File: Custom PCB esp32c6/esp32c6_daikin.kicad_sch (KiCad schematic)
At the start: 24 parts, among them J2 Conn_01x05, Q1 BSS138PS, U1 TPS562246, U2 XIAO-ESP32-C6

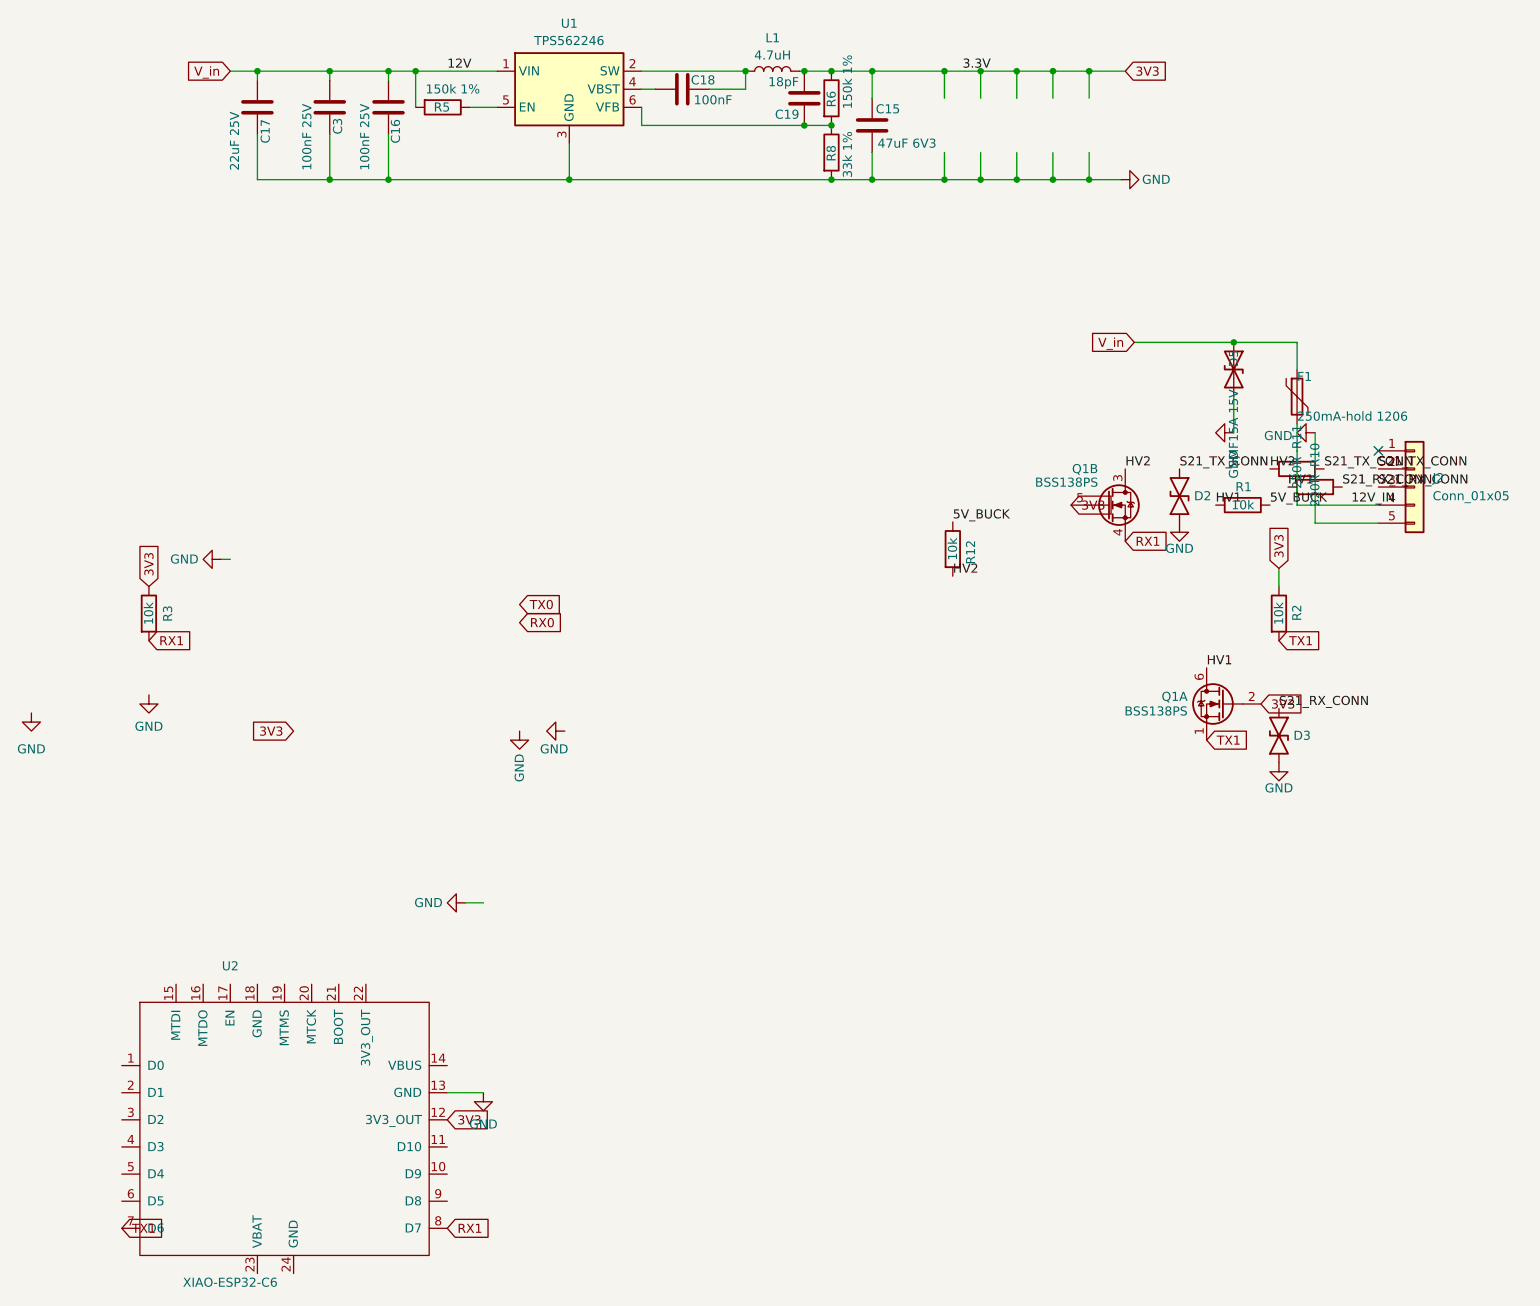
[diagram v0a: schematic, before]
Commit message: feat(xiao-sch): buck 5V re-tune, VBUS isolation diode, cap re-home
Re-tune TPS562246 buck 3.3V->5.0V, split the merged 3V3 net, add the
USB-back-feed isolation Schottky, and clear all ERC errors (29->0).

Divider (datasheet SLUSFG8A Vref=0.600V typ, Table 7-2 5V row):
  R6 150k->220k, R8 33k->30k, C19 18pF->47pF  =>  Vout=0.600*(1+220/30)=5.000V.
  Note: the brief's "Vref~0.804V, Vout~4.46V" premise was wrong; Vref is 0.600V
  and the old divider gave 3.33V (this was a 3.3V buck). Confirmed 5V within the
  0.6-7V output range and 12V within the 4.2-17V input range.

Net split (verified by netlist node-set, not coordinates):
  Buck-output rail label 3V3(global)->5V_BUCK(local), merging with R1/R12; also
  renamed a masked leftover local label 3.3V->5V_BUCK that would otherwise have
  hijacked the net name. XIAO 3V3_OUT (U2.12) stays on 3V3. Result: three
  distinct nets 5V_BUCK / VBUS / 3V3.

VBUS isolation + filtering:
  D6 (PMEG2005, SOD-123) anode->5V_BUCK, cathode->VBUS; XIAO pin14 on VBUS only.
  C15 47uF 6V3->10V (was 79% derated on 5V), re-homed to 5V_BUCK. Ferrite FB1
  (600R, >=500mA) + C20 10uF as a damped shunt off 5V_BUCK (in-line filtering
  would move the diode anode off 5V_BUCK, which the design gate forbids).
  Input caps C3/C16/C17 (25V) and bootstrap C18 untouched.

ERC cleanup to 0 errors: deleted orphan GND #PWR01/02/013/015 and dangling
labels TX0/RX0/extra-3V3; PWR_FLAGs on V_in and GND; no_connect on 19 unused
XIAO pins; wired XIAO VBUS pad.
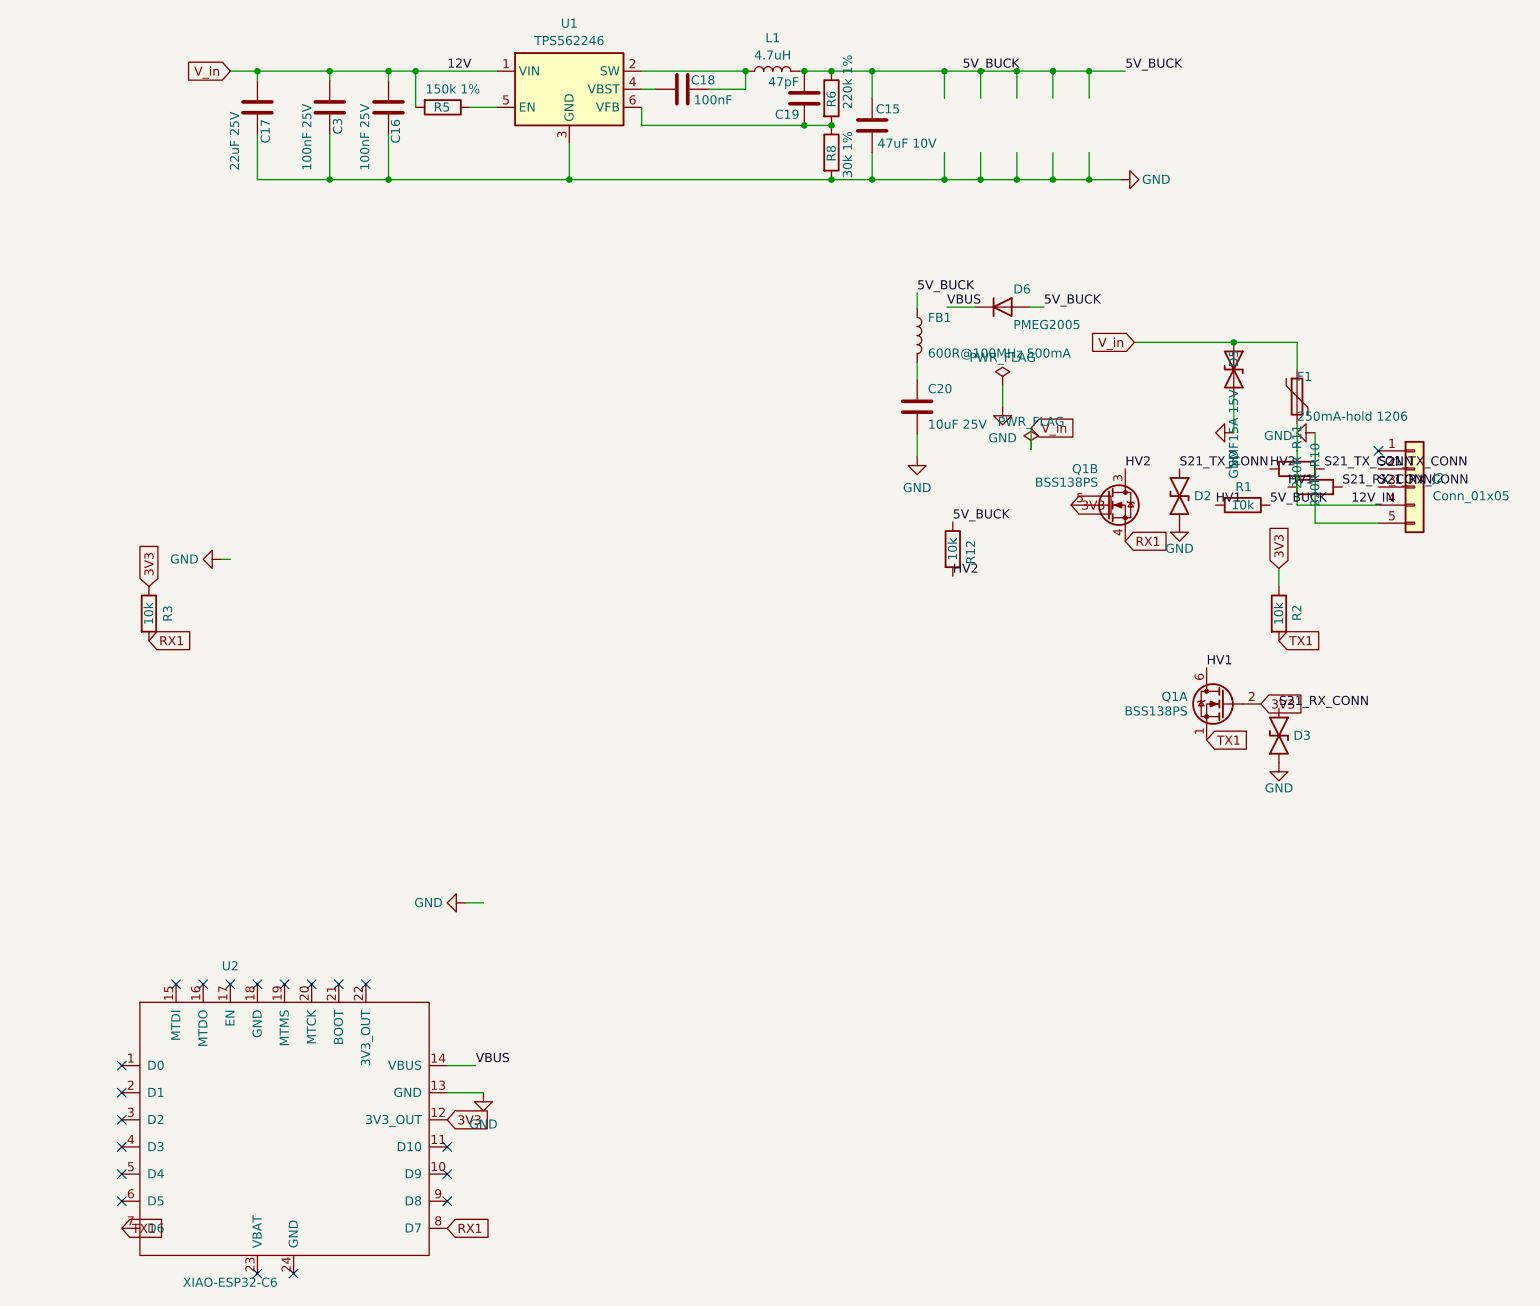
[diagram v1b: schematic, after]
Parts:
- added C20: 10uF 25V, easyeda2kicad:C0805, symbol Device:C
- added D6: PMEG2005, Diode_SMD:D_SOD-123, symbol Device:D
- added FB1: 600R@100MHz 500mA, Inductor_SMD:L_0805_2012Metric, symbol Device:L
- C15: value 47uF 6V3 -> 47uF 10V
- C19: value 18pF -> 47pF
- R6: value 150k 1% -> 220k 1%
- R8: value 33k 1% -> 30k 1%
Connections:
- net 3V3: no longer C15.1, C19.2, L1.2, R6.1
- net 5V_BUCK: now also C15.1, C19.2, L1.2, R6.1, D6.2 (A), FB1.1
- net GND: now also C20.2
- net VBUS: now reaches U2.14 (VBUS)
- net VBUS: now also D6.1 (K)
- new net: C20.1, FB1.2
- no-connect marks 1 -> 20

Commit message: fix(xiao-sch): drop dead-end ferrite, decouple XIAO VBUS with C20
FB1 (ferrite) fed C20 in a shunt off 5V_BUCK that dead-ended at GND -
it filtered nothing downstream, flagged by two EDA reviewers. Deleted
FB1 and re-homed C20 to decouple the XIAO VBUS pad (post-Schottky D6)
instead: C20.1 -> VBUS, C20.2 -> GND (unchanged).

Also cleaned up 10 dangling wire-endpoint stubs left from the Task 5
buck-rail rehoming (verified via ERC ground truth, not just the
approximate coordinate list in the task brief - found a 5th affected
column the brief missed), and corrected U1's stale TPS562246
description (580kHz/0.804V-7V -> 1.28MHz/0.6V-7V per datasheet
SLUSFG8A) that had misled an earlier review.

Netlist-verified: /VBUS = C20.1 D6.1 U2.14, /5V_BUCK loses FB1.1 but
keeps all other members, 3V3/5V_BUCK/VBUS stay three distinct nets,
shifter nets (TX1/RX1/HV1/HV2) unchanged. ERC 0 errors,
unconnected_wire_endpoint warnings 12 -> 2 (remaining 2 pre-existing,
unrelated, out of scope).
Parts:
- removed FB1: 600R@100MHz 500mA, Inductor_SMD:L_0805_2012Metric, symbol Device:L
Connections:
- net VBUS: now also C20.1
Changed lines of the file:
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@@
 	(wire
 		(pts
-			(xy 184.15 34.29) (xy 184.15 38.1)
-		)
-		(stroke
-			(width 0)
-			(type default)
-		)
-	)
-	(wire
-		(pts
 			(xy 179.07 38.1) (xy 184.15 38.1)
 		)
@@
 	(wire
 		(pts
-			(xy 163.83 22.86) (xy 163.83 26.67)
-		)
-		(stroke
-			(width 0)
-			(type default)
-		)
-	)
-	(wire
-		(pts
-			(xy 168.91 34.29) (xy 168.91 38.1)
-		)
-		(stroke
-			(width 0)
-			(type default)
-		)
-	)
-	(wire
-		(pts
 			(xy 168.91 38.1) (xy 173.99 38.1)
 		)
@@
 	(wire
 		(pts
-			(xy 168.91 22.86) (xy 168.91 26.67)
-		)
-		(stroke
-			(width 0)
-			(type default)
-		)
-	)
-	(wire
-		(pts
 			(xy 210.82 92.71) (xy 210.82 95.25)
 		)
@@
 	(wire
 		(pts
-			(xy 173.99 22.86) (xy 173.99 26.67)
-		)
-		(stroke
-			(width 0)
-			(type default)
-		)
-	)
-	(wire
-		(pts
 			(xy 67.31 22.86) (xy 67.31 24.13)
 		)
@@
 	(wire
 		(pts
-			(xy 173.99 34.29) (xy 173.99 38.1)
-		)
-		(stroke
-			(width 0)
-			(type default)
-		)
-	)
-	(wire
-		(pts
 			(xy 77.47 22.86) (xy 85.725 22.86)
 		)
@@
 	(wire
 		(pts
-			(xy 179.07 34.29) (xy 179.07 38.1)
-		)
-		(stroke
-			(width 0)
-			(type default)
-		)
-	)
-	(wire
-		(pts
 			(xy 173.99 38.1) (xy 179.07 38.1)
 		)
@@
 	(wire
 		(pts
-			(xy 163.83 34.29) (xy 163.83 38.1)
-		)
-		(stroke
-			(width 0)
-			(type default)
-		)
-	)
-	(wire
-		(pts
-			(xy 184.15 22.86) (xy 184.15 26.67)
-		)
-		(stroke
-			(width 0)
-			(type default)
-		)
-	)
-	(wire
-		(pts
 			(xy 111.125 38.1) (xy 85.725 38.1)
 		)
@@
 	(wire
 		(pts
-			(xy 179.07 22.86) (xy 179.07 26.67)
-		)
-		(stroke
-			(width 0)
-			(type default)
-		)
-	)
-	(wire
-		(pts
 			(xy 213.36 76.2) (xy 213.36 83.82)
 		)
@@
 			)
 		)
-		(property "Description" "2A Synchronous Step-Down Voltage Regulator 580kHz, adjustable output voltage, 4.5-17V Input Voltage, 0.804V-7V Output Voltage, SOT-563"
+		(property "Description" "2A Synchronous Step-Down Voltage Regulator 1.28MHz, adjustable output voltage, 4.5-17V Input Voltage, 0.6V-7V Output Voltage, SOT-563"
 			(at 111.125 25.4 0)
 			(hide yes)
@@
 	)
 	(symbol
-		(lib_id "Device:L")
-		(at 160 60 0)
-		(unit 1)
-		(body_style 1)
-		(exclude_from_sim no)
-		(in_bom yes)
-		(on_board yes)
-		(in_pos_files yes)
-		(dnp no)
-		(property "Reference" "FB1"
-			(at 161.5 57.5 0)
-			(show_name no)
-			(do_not_autoplace no)
-			(effects
-				(font
-					(size 1.27 1.27)
-				)
-				(justify left)
-			)
-		)
-		(property "Value" "600R@100MHz 500mA"
-			(at 161.5 62.5 0)
-			(show_name no)
-			(do_not_autoplace no)
-			(effects
-				(font
-					(size 1.27 1.27)
-				)
-				(justify left)
-			)
-		)
-		(property "Footprint" "Inductor_SMD:L_0805_2012Metric"
-			(at 160 60 0)
-			(hide yes)
-			(show_name no)
-			(do_not_autoplace no)
-			(effects
-				(font
-					(size 1.27 1.27)
-				)
-			)
-		)
-		(property "Datasheet" ""
-			(at 160 60 0)
-			(hide yes)
-			(show_name no)
-			(do_not_autoplace no)
-			(effects
-				(font
-					(size 1.27 1.27)
-				)
-			)
-		)
-		(property "Description" "Ferrite bead"
-			(at 160 60 0)
-			(hide yes)
-			(show_name no)
-			(do_not_autoplace no)
-			(effects
-				(font
-					(size 1.27 1.27)
-				)
-			)
-		)
-		(pin "1"
-		)
-		(pin "2"
-		)
-		(instances
-			(project "esp32c6_daikin"
-				(path "/46c350bb-7de4-4e81-aafd-4af55e37aab0"
-					(reference "FB1")
-					(unit 1)
-				)
-			)
-		)
-	)
-	(wire
-		(pts
-			(xy 160 56.19) (xy 160 54.0)
-		)
-		(stroke
-			(width 0)
-			(type default)
-		)
-	)
-	(label "5V_BUCK"
-		(at 160 54.0 0)
-		(effects
-			(font
-				(size 1.27 1.27)
-			)
-			(justify left bottom)
-		)
-	)
-	(symbol
 		(lib_id "Device:C")
 		(at 160 70 0)
@@
 		)
 	)
+	(label "VBUS"
+		(at 160 63.81 0)
+		(effects
+			(font
+				(size 1.27 1.27)
+			)
+			(justify left bottom)
+		)
+	)

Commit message: fix(xiao-sch): assign D2/D3 sourceable values
D2/D3 protect the S21 TX/RX lines to GND (LCSC C5137770 = GOODWORK
ES05D1MC10, bidirectional 5V ESD/TVS, DFN1006-2L). Value fields were
blank; set to 'ESD 5V bidir'. Metadata only, no wiring change: netlist
node-sets byte-identical (36 nets, 0 changed), ERC 0 errors, DRC
schematic-parity 0.
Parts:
- D2, D3: value (none) -> ESD 5V bidir
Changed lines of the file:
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@@
 			)
 		)
-		(property "Value" ""
+		(property "Value" "ESD 5V bidir"
 			(at 210.82 116.205 0)
 			(show_name no)
@@
 			)
 		)
-		(property "Value" ""
+		(property "Value" "ESD 5V bidir"
 			(at 196.85 82.55 0)
 			(show_name no)

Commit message: fix(xiao-sch): correct stale rev-b LCSC part numbers
The XIAO board inherited four LCSC assignments from rev-b whose parts no
longer match the updated values, plus one obsolete part. JLC and any
regenerated BOM assemble by LCSC number, so these would mis-build the board:

  R6  C22807 (150k)  -> C22961  (220k 1% 0603)   buck FB top, sets Vout
  R8  C25779 (33k)   -> C138008 (30k 1% 0402)    buck FB bottom, sets Vout
  C15 C16780 (6.3V)  -> C2292827 (47uF 10V 0805) buck out; 6.3V fails DC-bias
  C19 C1549  (18pF)  -> C84706  (47pF C0G 0402)  buck feedforward
  C17 C45783 (obsolete) -> C398931 (22uF 25V 0805 Murata GRT, in stock)

Metadata only, no wiring change: netlist node-sets byte-identical (36 nets,
0 changed), ERC 0 errors, DRC schematic-parity 0. Values web-verified against
LCSC product pages.
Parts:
- C15: LCSC C16780 -> C2292827
- C17: LCSC C45783 -> C398931
- C19: LCSC C1549 -> C84706
- R6: LCSC C22807 -> C22961
- R8: LCSC C25779 -> C138008
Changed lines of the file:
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@@
 			)
 		)
-		(property "LCSC" "C22807"
+		(property "LCSC" "C22961"
 			(at 147.955 26.67 0)
 			(hide yes)
@@
 			)
 		)
-		(property "LCSC" "C25779"
+		(property "LCSC" "C138008"
 			(at 147.955 34.29 0)
 			(hide yes)
@@
 			)
 		)
-		(property "LCSC" "C16780"
+		(property "LCSC" "C2292827"
 			(at 153.67 30.48 0)
 			(hide yes)
@@
 			)
 		)
-		(property "LCSC" "C1549"
+		(property "LCSC" "C84706"
 			(at 144.145 26.67 90)
 			(hide yes)
@@
 			)
 		)
-		(property "LCSC" "C45783"
+		(property "LCSC" "C398931"
 			(at 67.31 27.94 0)
 			(hide yes)

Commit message: chore(xiao): final-review metadata cleanup
Applies the mechanical items from final review that survived verification:

1. LCSC fields added: D6 -> C96233, C20 -> C15850 (metadata only).

2. NOT applied. Review flagged two micro wire stubs (0.0127mm/0.0254mm,
   UUIDs 30fba69b.../d927969b...) as unconnected_wire_endpoint ERC
   warnings safe to delete. Verified false: each stub is the sole
   graphical connection for a GND power symbol (#PWR06, #PWR017).
   Deleting them leaves those pins with zero attached wires, which
   flips ERC from 0 errors/72 warnings to 2 errors (pin_not_connected).
   The <nets> netlist section is unaffected either way (power-symbol
   global-label net forms independently of the local wire), but the
   ERC error-count gate fails, so the stubs stay.

3. NOT applied. Review claimed the XIAO_antenna_keepout zone was
   via-free, so switching vias allowed -> not_allowed was believed
   copper-inert. DRC shows a GND via at (155.5, 93.5) sitting inside
   that exact zone; the edit produces 1 gating DRC error
   (items_not_allowed). Board file left byte-identical to pre-edit.

ERC: 0 errors / 72 warnings, unchanged before/after (item 1 only).
Gating DRC (--severity-error): 0/0, unchanged (item 3 reverted, board
untouched).
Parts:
- C20: LCSC (none) -> C15850
- D6: LCSC (none) -> C96233
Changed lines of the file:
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@@
+			)
+		)
+		(property "LCSC" "C96233"
+			(at 172 56 0)
+			(hide yes)
+			(show_name no)
+			(do_not_autoplace no)
+			(effects
+				(font
+					(size 1.27 1.27)
+				)
 			)
 		)
@@
 			(at 160 70 0)
 			(hide yes)
+			(show_name no)
+			(do_not_autoplace no)
+			(effects
+				(font
+					(size 1.27 1.27)
+				)
+			)
+		)
+		(property "LCSC" "C15850"
+			(at 160 70 0)
+			(hide yes)
